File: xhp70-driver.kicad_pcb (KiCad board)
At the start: 2 copper layers, 47.3 x 26.3 mm, 27 parts, among them J1 LEMO2, J2 AVR-ISP-6, Q1 Q_NMOS_GDS, U1 AL8871Q, U2 ATtiny85-20SU, U3 L7805

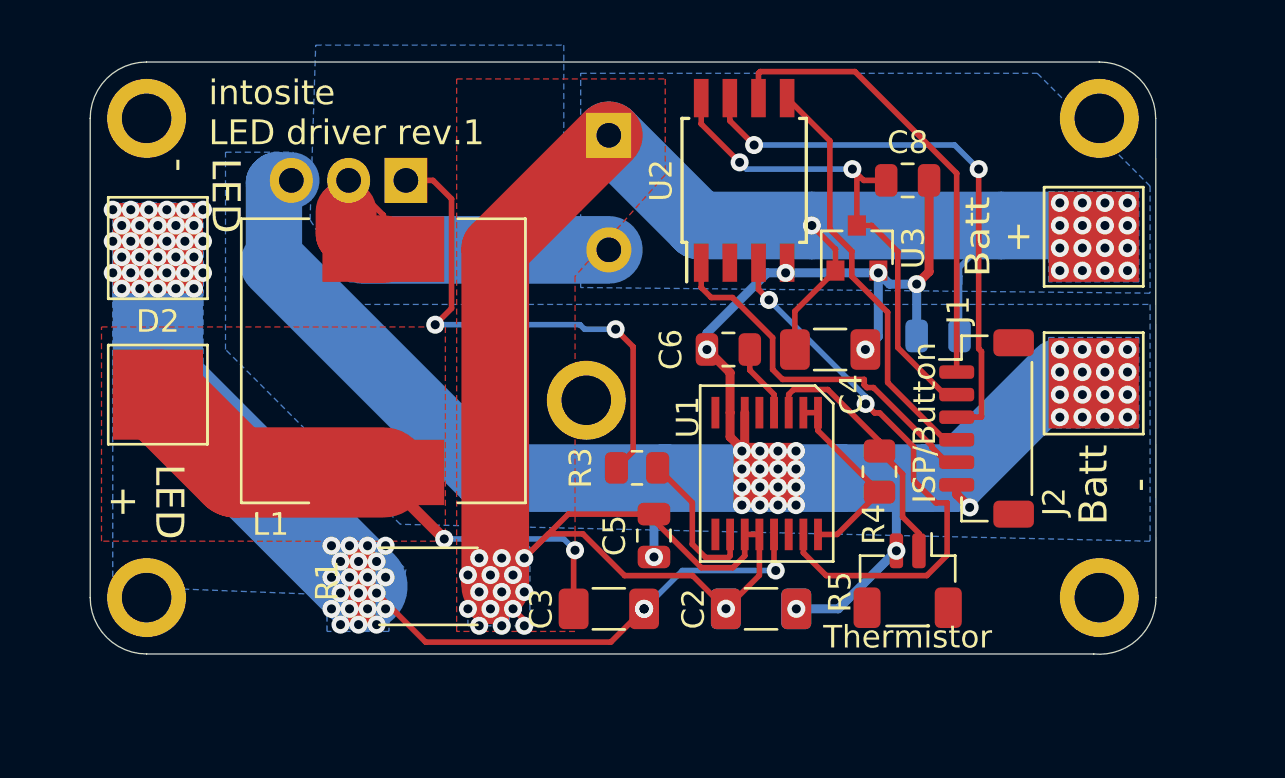
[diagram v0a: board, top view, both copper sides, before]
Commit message: Rev 2a - route NTC Thermistor to Attiny to control output
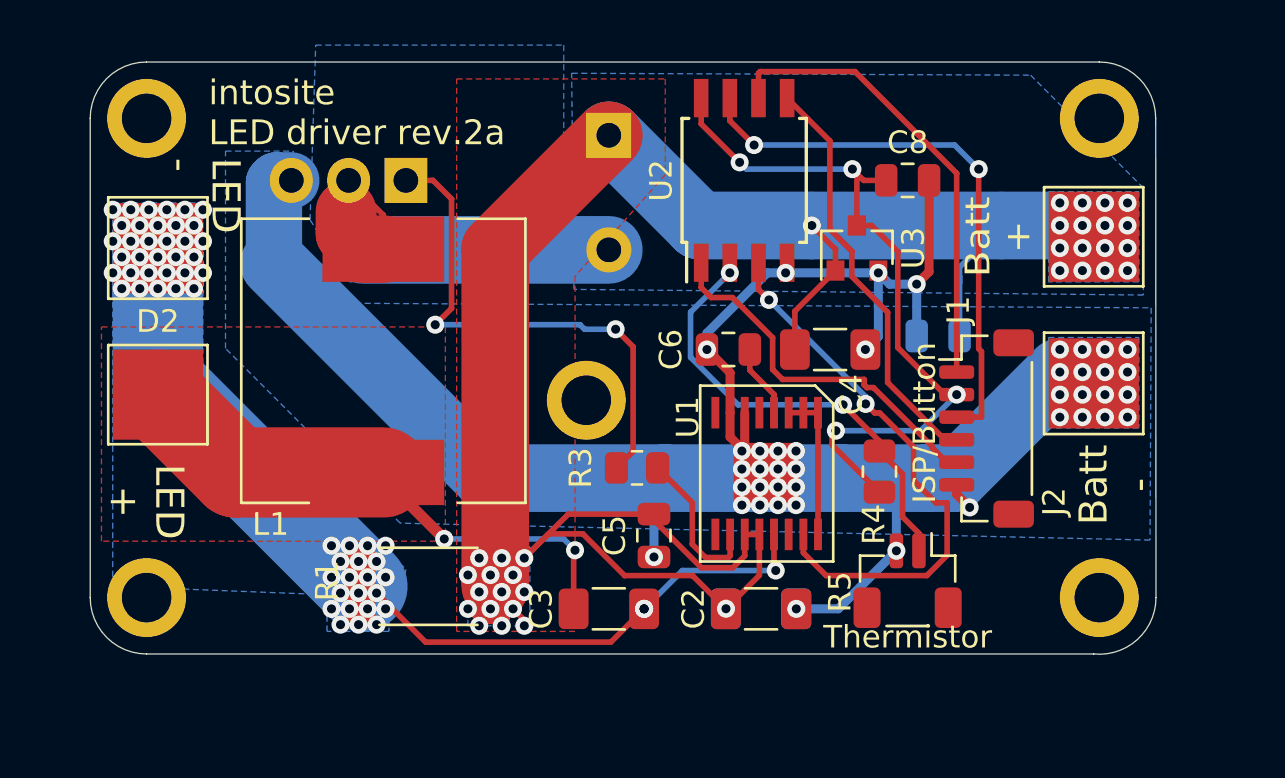
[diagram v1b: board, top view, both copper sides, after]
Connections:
- C8 pad 1: Net-(C8-Pad1) -> +5V
- J2 pad 2: Net-(C8-Pad1) -> +5V
- R4 pad 1: Net-(R4-Pad1) -> +5V
- R4 pad 2: Net-(R4-Pad2) -> NTC
- R5 pad 1: Net-(R4-Pad2) -> NTC
- U1 pad 1: Net-(R4-Pad1) -> Net-(U1-Pad1)
- U1 pad 16: Net-(R4-Pad1) -> Net-(U1-Pad1)
- U1 pad 2: Net-(R4-Pad1) -> Net-(U1-Pad1)
- U1 pad 3: Net-(R4-Pad2) -> Net-(U1-Pad1)
- U2 pad 2: Net-(U2-Pad2) -> NTC
- U2 pad 8: Net-(C8-Pad1) -> +5V
- U3 pad 3: Net-(C8-Pad1) -> +5V
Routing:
- net +5V: track 0.00 -> 32.9 mm, vias 0 -> 4
- net Net-(C8-Pad1): track 23.2 -> 0.00 mm, vias 2 -> 0
- net NTC: track 0.00 -> 20.4 mm, vias 0 -> 2
- net Net-(R4-Pad2): track 11.5 -> 0.00 mm
- net Net-(R4-Pad1): track 8.81 -> 0.00 mm
- net Net-(U1-Pad1): track 0.00 -> 6.70 mm
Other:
- board text added: "intosite LED driver rev.2a"
- board text removed: "intosite LED driver rev.1"
- board text removed: "intosite LED driver rev.1b"

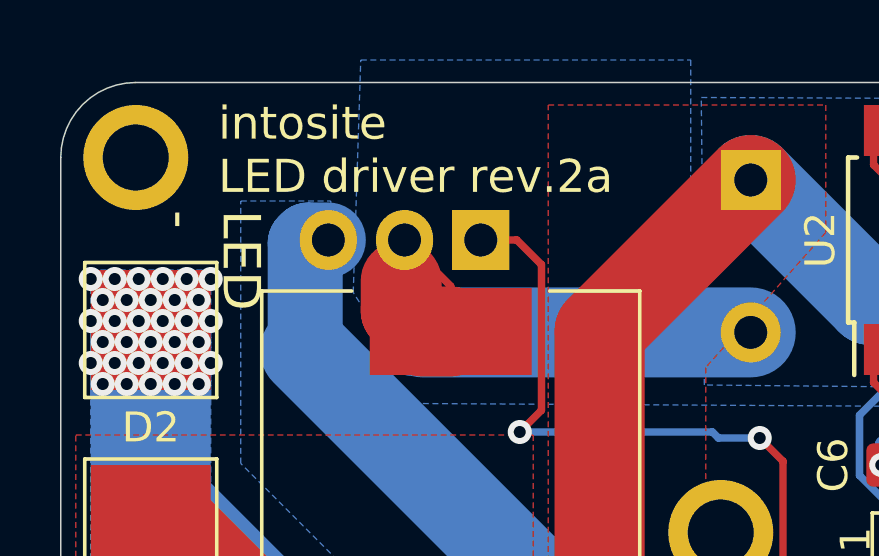
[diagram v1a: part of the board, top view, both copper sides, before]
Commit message: L7805 schematic pinout is wrong. Needs reroute. `
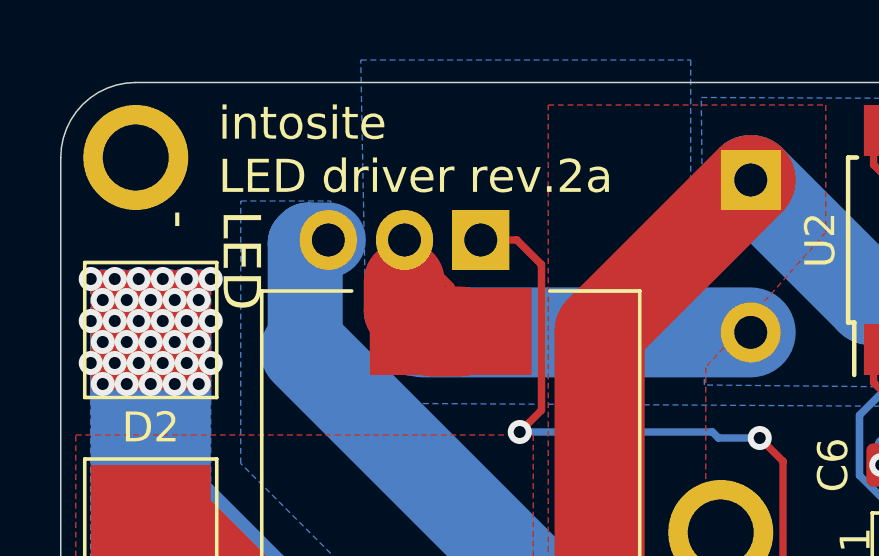
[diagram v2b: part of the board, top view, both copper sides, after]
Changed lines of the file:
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@@
   (via (at 114.6 60.1) (size 0.8) (drill 0.4) (layers F.Cu B.Cu) (net 2))
   (via (at 113.4 60.8) (size 0.8) (drill 0.4) (layers F.Cu B.Cu) (net 2))
-  (segment (start 123.347499 57.25) (end 123.347499 57.371216) (width 2.5) (layer B.Cu) (net 3))
-  (segment (start 123.347499 58.360001) (end 123.347499 57.25) (width 2.5) (layer B.Cu) (net 3))
+  (segment (start 123.45 57.260608) (end 123.45 57.381824) (width 2.5) (layer B.Cu) (net 3))
+  (segment (start 123.45 58.360001) (end 123.45 57.25) (width 2.5) (layer B.Cu) (net 3))
   (segment (start 124.067498 59.08) (end 123.347499 58.360001) (width 2.5) (layer B.Cu) (net 3))
-  (segment (start 135 59.08) (end 124.067498 59.08) (width 3) (layer B.Cu) (net 3))
-  (segment (start 124.037498 59.05) (end 123.347499 58.360001) (width 2.7) (layer F.Cu) (net 3))
-  (segment (start 123.347499 58.360001) (end 123.347499 57.371216) (width 2.7) (layer F.Cu) (net 3))
-  (segment (start 125 59.05) (end 124.037498 59.05) (width 3) (layer F.Cu) (net 3))
+  (segment (start 124.389999 59.05) (end 123.7 58.360001) (width 2.7) (layer F.Cu) (net 3))
+  (segment (start 123.45 58.360001) (end 123.45 57.371216) (width 2.7) (layer F.Cu) (net 3))
+  (segment (start 125.312502 59.05) (end 124.35 59.05) (width 3) (layer F.Cu) (net 3))
   (segment (start 125 57.54) (end 123.46 56) (width 0.25) (layer F.Cu) (net 3))
   (segment (start 125 59.05) (end 125 57.54) (width 0.25) (layer F.Cu) (net 3))
+  (segment (start 135 59.08) (end 124.067498 59.08) (width 3) (layer B.Cu) (net 3))
   (via (at 127.3 62.4) (size 0.8) (drill 0.4) (layers F.Cu B.Cu) (net 4))
   (segment (start 128.025001 61.674999) (end 127.3 62.4) (width 0.25) (layer F.Cu) (net 4))
@@
     (polygon
       (pts
-        (xy 133 60.5) (xy 123.5 60.5) (xy 121.75 57.75) (xy 122 50) (xy 133 50)
-      )
-    )
+        (xy 133 60.5) (xy 123.5 60.5) (xy 122.15 57.8) (xy 122 50) (xy 133 50)
+      )
+    )

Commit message: Redo. Same as rev.2b
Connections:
- net Net-(J2-Pad1) renamed EC_A
- net Net-(J2-Pad3) renamed EC_B
- net Net-(J2-Pad4) renamed EC_Int
- U3 pad 1: Batt+ -> GND
- U3 pad 2: GND -> +5V
- U3 pad 3: +5V -> Batt+
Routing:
- net Batt+: track 87.5 -> 86.7 mm, vias 33 -> 34
- net Net-(D1-Pad2): vias 0 -> 22
- net Net-(C3-Pad2): vias 57 -> 96
- added copper zone on F.Cu, net GND
- added copper zone on F.Cu, net Net-(C3-Pad2)
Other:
- board text added: "intosite LED driver rev.2c"
- board text removed: "intosite LED driver rev.2a"

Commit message: Changed LDO to 78L05 linear voltage regulator
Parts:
- U3: value L7805 -> 78L05-SOT-23
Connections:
- U3 pad 1: GND -> +5V
- U3 pad 2: +5V -> Batt+
- U3 pad 3: Batt+ -> GND
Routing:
- net GND: track 91.3 -> 99.4 mm, vias 41 -> 40
- net Batt+: track 86.7 -> 89.0 mm
- net +5V: track 33.2 -> 35.1 mm
- net EC_Int: track 18.8 -> 20.1 mm

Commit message: Revised sense resistor placement
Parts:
- R2: moved to F.Cu
- moved Q1 4.00 mm to (126.0, 52.0)
- moved R2 4.00 mm to (127.0, 70.0)
- moved L1 3.59 mm to (124.5, 60.5)
- moved D2 2.24 mm to (114.2, 64.2), turned to 270 degrees
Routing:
- net Net-(D1-Pad2): track 19.8 -> 14.3 mm, vias 22 -> 26
- net Net-(C3-Pad1): track 24.1 -> 28.5 mm
- net GND: track 99.4 -> 103.2 mm
- net Net-(C3-Pad2): track 40.3 -> 36.6 mm, vias 96 -> 4
- net Net-(Q1-Pad1): track 23.1 -> 26.4 mm
- net Batt+: track 89.0 -> 85.9 mm, vias 34 -> 19
- removed copper zone on B.Cu, net Net-(C3-Pad2)
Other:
- board text added: "intosite LED driver rev.2d"
- board text removed: "intosite LED driver rev.2c"
